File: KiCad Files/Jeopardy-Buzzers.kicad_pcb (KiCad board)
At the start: 2 copper layers, 17 parts, among them U1 CH32V003FxUx, U2 CH340N, U3 NRF24L01_Breakout, U5 AMS1117-3.3, Y1 Crystal_24MHz

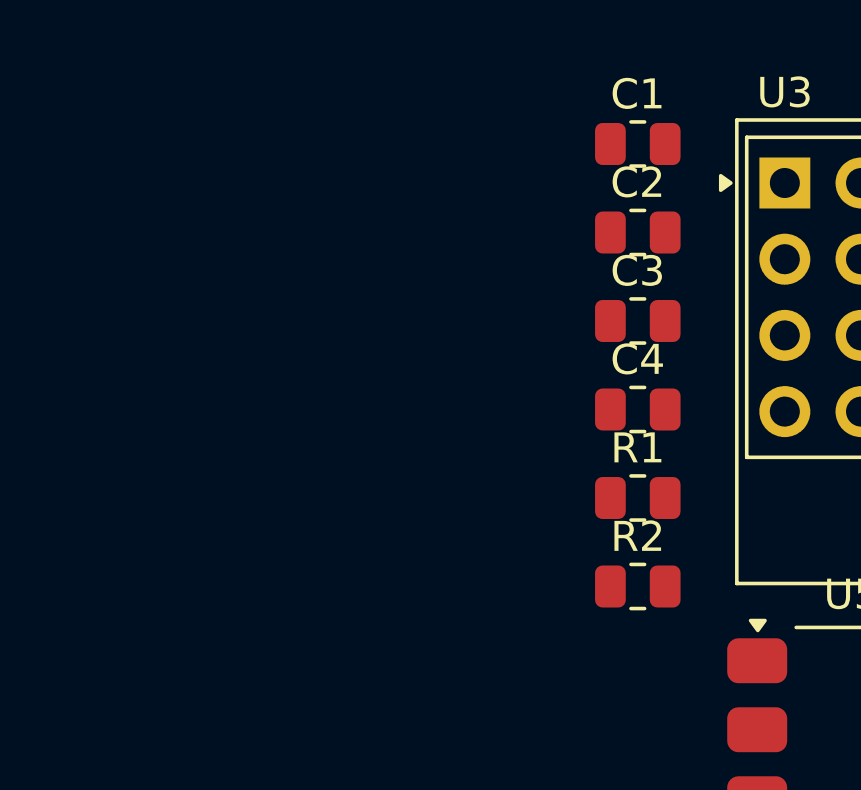
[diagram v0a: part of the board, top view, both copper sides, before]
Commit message: Added step files, and finished usb footprint
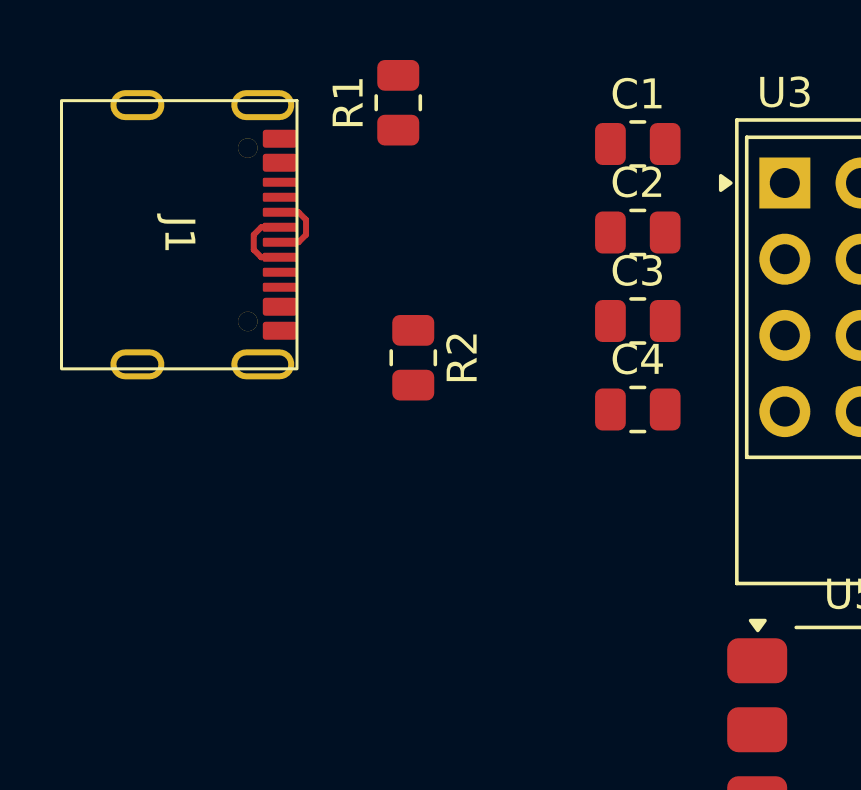
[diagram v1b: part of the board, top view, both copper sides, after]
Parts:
- added J1: USB_C_Receptacle, Library:Usb-C, F.Cu at (22.9, 29.5)
- moved R1 15.4 mm to (26.2, 25.1), turned to 90 degrees
- moved R2 10.7 mm to (26.8, 33.6), turned to -90 degrees
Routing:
- net Net-(D5-K): track 0.00 -> 2.45 mm
- net Net-(D4-K): track 0.00 -> 2.45 mm

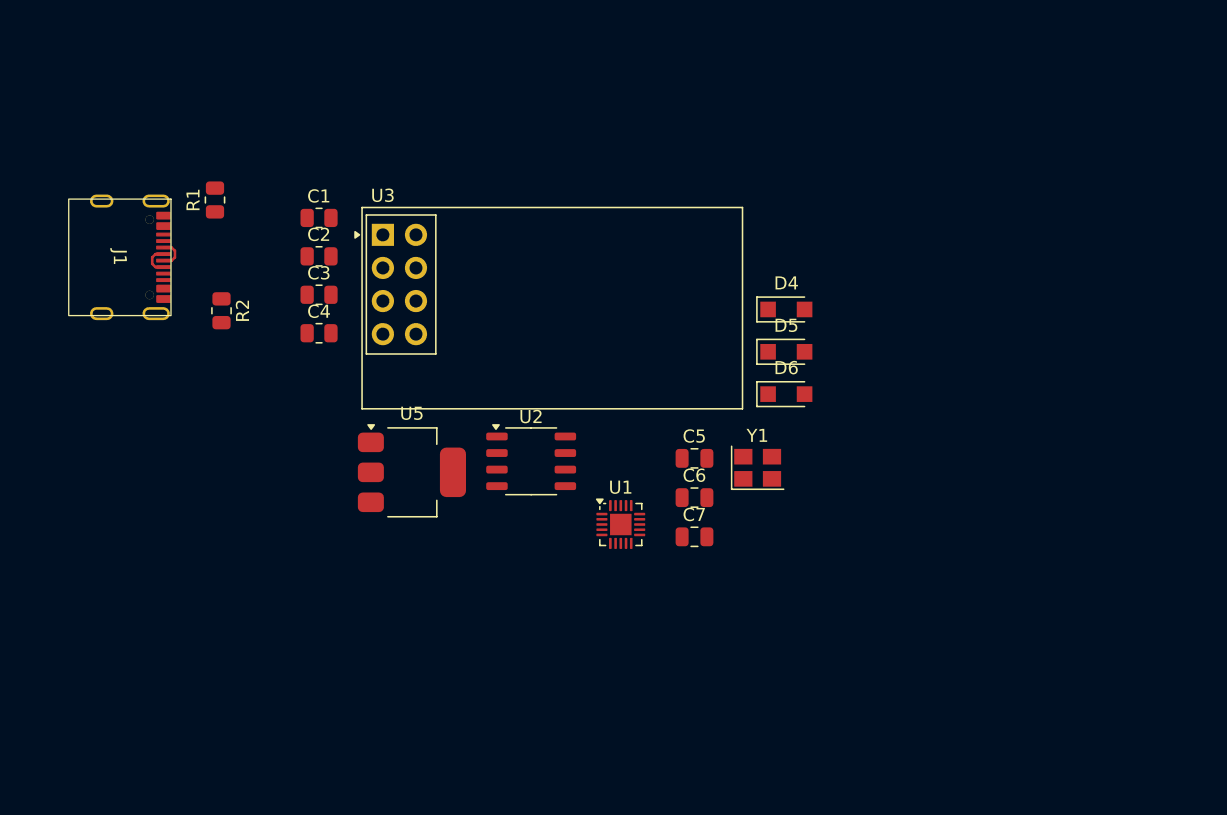
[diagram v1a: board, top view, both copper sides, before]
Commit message: Changed footprints around, also added connectors
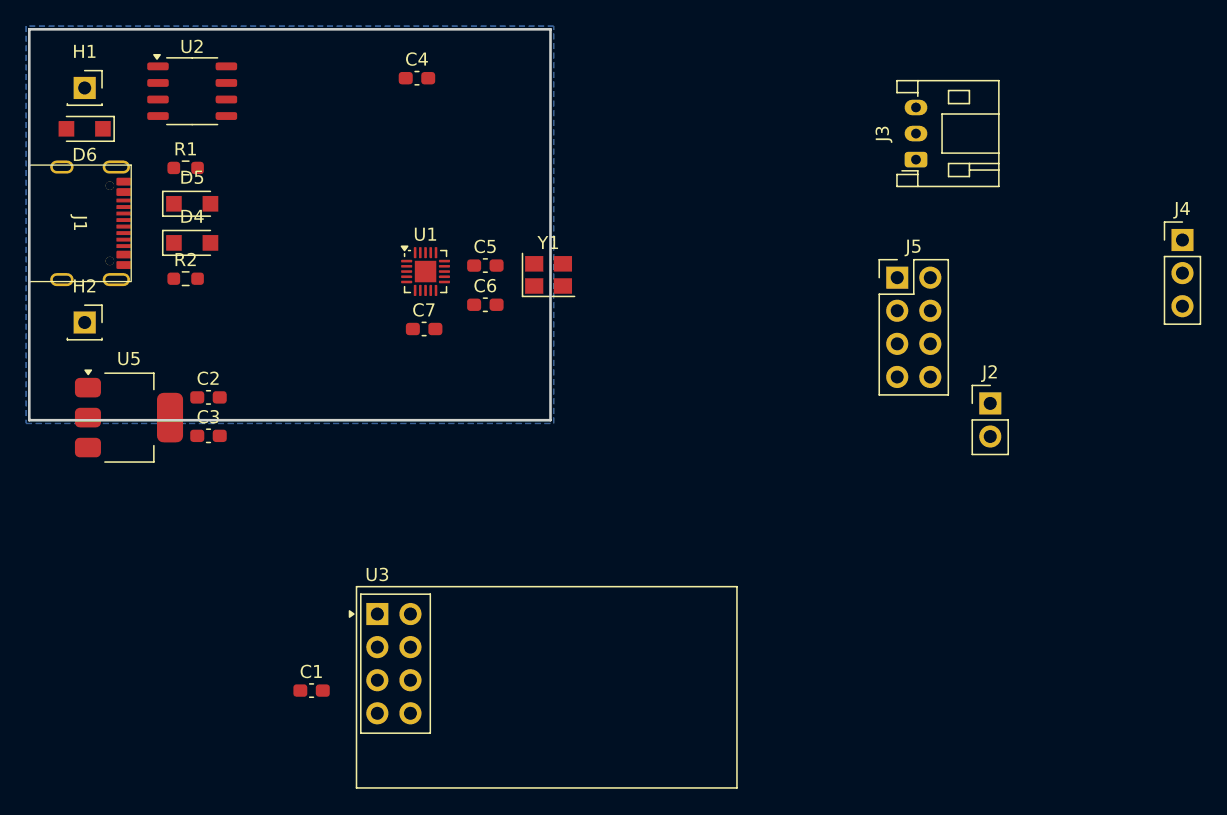
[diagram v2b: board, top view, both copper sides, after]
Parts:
- added H1: MountingHole_Pad, Connector_PinSocket_2.54mm:PinSocket_1x01_P2.54mm_Vertical, F.Cu at (16.2, 16.5)
- added H2: MountingHole_Pad, Connector_PinSocket_2.54mm:PinSocket_1x01_P2.54mm_Vertical, F.Cu at (16.2, 34.5)
- added J2: Conn_01x02_Pin, Connector_PinHeader_2.54mm:PinHeader_1x02_P2.54mm_Vertical, F.Cu at (85.8, 40.7)
- added J3: Conn_01x03_Socket, Connector_JST:JST_PH_S3B-PH-K_1x03_P2.00mm_Horizontal, F.Cu at (80.0, 22.0)
- added J4: Conn_01x03_Socket, Connector_PinHeader_2.54mm:PinHeader_1x03_P2.54mm_Vertical, F.Cu at (100.5, 28.2)
- added J5: Conn_02x04_Odd_Even, Connector_PinHeader_2.54mm:PinHeader_2x04_P2.54mm_Vertical, F.Cu at (78.6, 31.1)
- C1, C2, C3, C4: footprint Resistor_SMD:R_0805_2012Metric -> Capacitor_SMD:C_0603_1608Metric_Pad1.08x0.95mm_HandSolder
- C5, C6, C7: footprint Capacitor_SMD:C_0805_2012Metric -> Capacitor_SMD:C_0603_1608Metric_Pad1.08x0.95mm_HandSolder
- J1: value USB_C_Receptacle -> USB_C_Receptacle_USB2.0_14P
- R1, R2: footprint Resistor_SMD:R_0805_2012Metric -> Resistor_SMD:R_0603_1608Metric_Pad0.98x0.95mm_HandSolder
- moved D6 57.6 mm to (16.2, 19.6), turned to 180 degrees
- moved D5 47.0 mm to (24.5, 25.4)
- moved D4 45.9 mm to (24.5, 28.4)
- moved U2 38.5 mm to (24.5, 16.8)
- moved C1 36.3 mm to (33.7, 62.8)
- moved U3 29.1 mm to (38.7, 56.9)
- moved C7 26.2 mm to (42.3, 35.0)
- moved U1 24.5 mm to (42.4, 30.6)
- moved U5 22.1 mm to (19.6, 41.8)
- moved C5 21.8 mm to (47.0, 30.1)
- moved Y1 21.8 mm to (51.9, 30.9)
- moved C6 21.8 mm to (47.0, 33.1)
- moved C4 21.0 mm to (41.8, 15.8)
- moved C3 13.8 mm to (25.8, 43.2)
- moved C2 13.8 mm to (25.8, 40.2)
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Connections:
- net Net-(D4-K) renamed USB_D+
- net Net-(D5-K) renamed USB_D-
- C7 pad 2: Net-(U1-VDD) -> +5V
- J1 pad A8: unconnected-(J1-SBU1-PadA8) -> (no net)
- J1 pad B8: unconnected-(J1-SBU2-PadB8) -> (no net)
- U1 pad 1: unconnected-(U1-PD7-Pad1) -> WS2812_LED
- U1 pad 10: unconnected-(U1-PC3-Pad10) -> MCU_PC3
- U1 pad 15: unconnected-(U1-PD1-Pad15) -> MCU_SWIO
- U1 pad 16: unconnected-(U1-PD2-Pad16) -> MCU_PD2
- U1 pad 17: unconnected-(U1-PD3-Pad17) -> MCU_PD3
- U1 pad 18: unconnected-(U1-PD4-Pad18) -> MCU_PD4
- U1 pad 5: unconnected-(U1-PD0-Pad5) -> Net-(J2-Pin_2)
- U1 pad 6: Net-(U1-VDD) -> +5V
- U1 pad 8: unconnected-(U1-PC1-Pad8) -> MCU_PC1
- U1 pad 9: unconnected-(U1-PC2-Pad9) -> MCU_PC2
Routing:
- net USB_D-: track 2.45 -> 0.00 mm
- net USB_D+: track 2.45 -> 0.00 mm
- added copper zone on B.Cu, net GND
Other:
- board outline added: 40 x 30 mm

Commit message: moved parts around and started placing planes
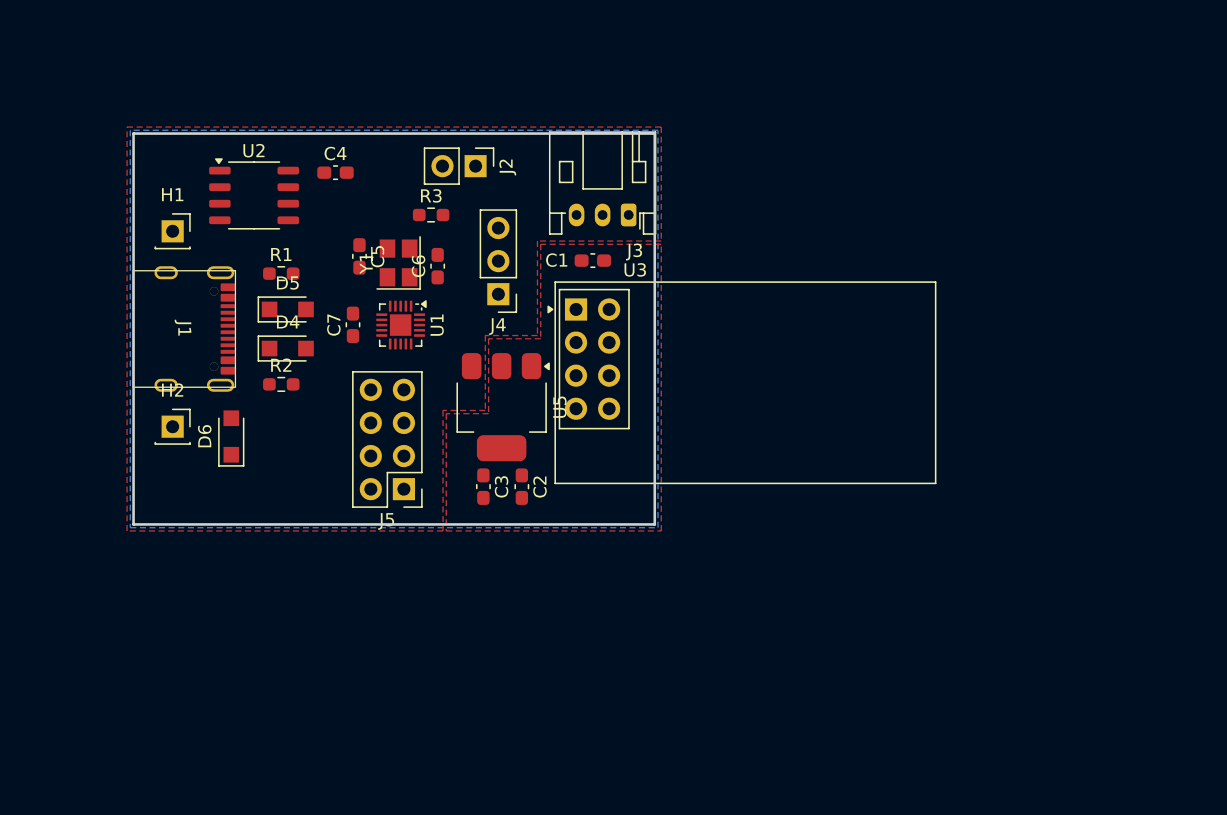
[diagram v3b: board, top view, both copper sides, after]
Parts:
- added R3: 10k, Resistor_SMD:R_0603_1608Metric_Pad0.98x0.95mm_HandSolder, F.Cu at (42.8, 26.2)
- moved J4 52.7 mm to (48.0, 32.3), turned to 180 degrees
- moved J2 43.5 mm to (46.2, 22.5), turned to -90 degrees
- moved J5 41.2 mm to (40.8, 47.3), turned to 180 degrees
- moved C1 39.4 mm to (55.2, 29.8), turned to 180 degrees
- moved U5 28.6 mm to (48.2, 41.0), turned to -90 degrees
- moved U3 27.9 mm to (54.0, 33.5)
- moved D6 26.2 mm to (27.5, 43.2), turned to 90 degrees
- moved C2 25.0 mm to (49.8, 47.1), turned to -90 degrees
- moved J3 22.5 mm to (58.0, 26.2), turned to 180 degrees
- moved C3 21.5 mm to (46.9, 47.1), turned to -90 degrees
- moved H1 12.9 mm to (23.0, 27.5)
- moved Y1 11.5 mm to (40.3, 29.9), turned to 90 degrees
- moved J1 11.4 mm to (27.8, 35.0)
- moved D4 10.9 mm to (31.8, 36.5)
- moved D5 10.9 mm to (31.8, 33.5)
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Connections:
- J5 pad 3: MCU_PC1 -> MCU_PC0
- J5 pad 5: MCU_PC2 -> MCU_PC1
- J5 pad 7: MCU_PC3 -> MCU_PC2
- U1 pad 10: MCU_PC3 -> MCU_SPI_CS
- U1 pad 7: MCU_SPI_CS -> MCU_PC0
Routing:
- added copper zone on F.Cu, net +3V3
- added copper zone on F.Cu, net +5V

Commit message: routed most of the traces, just need to pass ERC/DRC
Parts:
- moved J5 4.30 mm to (41.0, 43.0), turned to -90 degrees
- moved J4 3.72 mm to (49.0, 28.8), turned to 0 degrees
- moved J3 0.56 mm to (57.8, 26.8)
- moved C5 0.55 mm to (37.0, 29.9)
- moved D4 0.51 mm to (32.4, 36.5)
- moved D5 0.51 mm to (32.4, 33.5)
- moved R1 0.51 mm to (31.9, 30.8)
- moved R2 0.51 mm to (31.9, 39.2)
- moved R3 0.51 mm to (42.8, 25.8)
- moved C6 0.45 mm to (43.8, 30.0)
- moved C4 0.25 mm to (35.5, 22.8)
- moved C7 0.23 mm to (36.8, 34.9)
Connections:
- J5 pad 3: MCU_PC0 -> MCU_PC2
- J5 pad 7: MCU_PC2 -> MCU_PC0
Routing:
- net MCU_SPI_CS: track 0.00 -> 31.4 mm
- net MCU_SPI_MOSI: track 0.00 -> 25.2 mm
- net MCU_PD4: track 0.00 -> 25.2 mm, vias 0 -> 1
- net MCU_UART_TX: track 0.00 -> 21.4 mm, vias 0 -> 2
- net NRF24L01_CE: track 0.00 -> 21.2 mm, vias 0 -> 1
- net MCU_PD3: track 0.00 -> 21.1 mm, vias 0 -> 1
- net +5V: track 0.00 -> 19.2 mm
- net MCU_SPI_CLK: track 0.00 -> 18.4 mm, vias 0 -> 1
- net MCU_UART_RX: track 0.00 -> 17.9 mm, vias 0 -> 2
- net WS2812_LED: track 0.00 -> 17.4 mm
- net MCU_PD2: track 0.00 -> 17.1 mm, vias 0 -> 1
- net Net-(J2-Pin_2): track 0.00 -> 16.1 mm, vias 0 -> 2
- net MCU_SPI_MISO: track 0.00 -> 15.6 mm
- net MCU_PC0: track 0.00 -> 13.3 mm
- net MCU_PC1: track 0.00 -> 10.1 mm
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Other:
- board text added: "+5v"
- board text added: "GND"

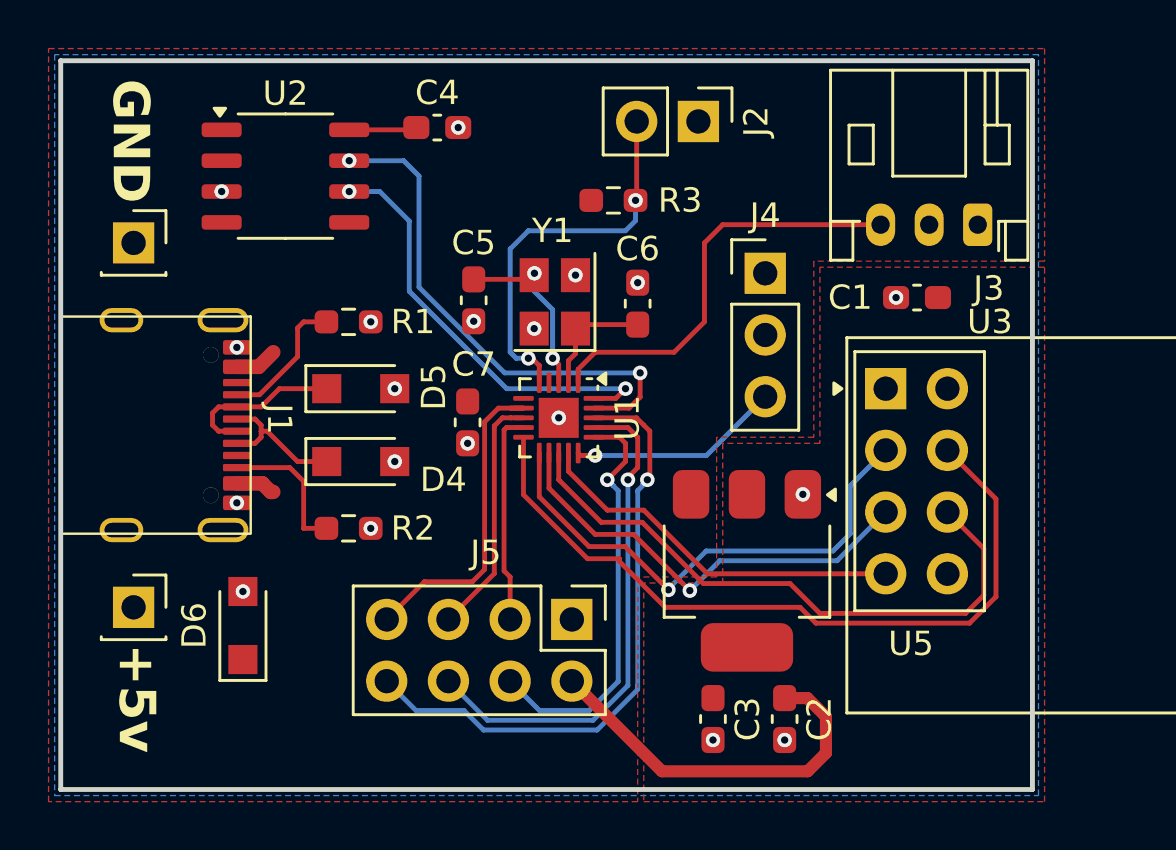
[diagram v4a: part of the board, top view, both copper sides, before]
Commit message: routed the USB and added my logo, text, and version number
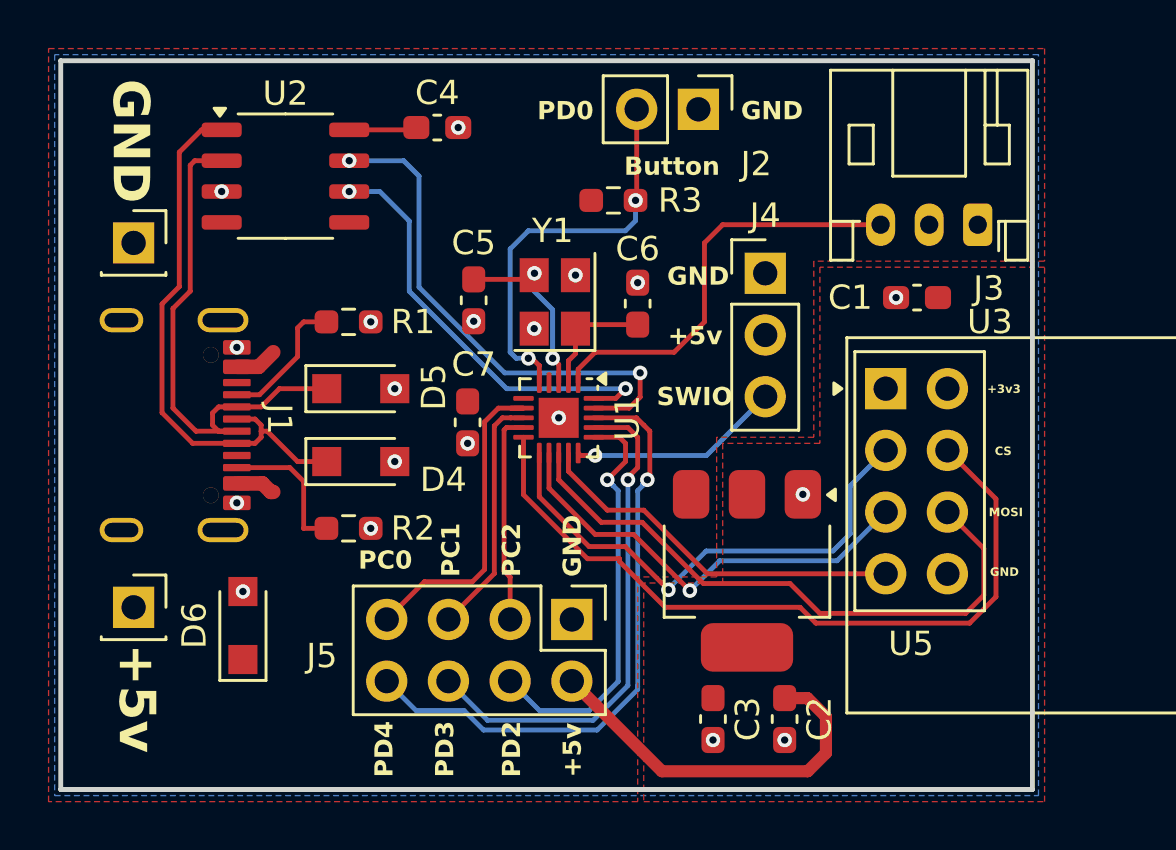
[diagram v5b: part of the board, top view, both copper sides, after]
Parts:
- added G***: LOGO, Library:PCB Logo (12.5x17), B.Cu at (35.5, 29.5)
- moved J2 0.50 mm to (46.2, 22.0)
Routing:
- net USB_D+: track 5.41 -> 22.2 mm
- net USB_D-: track 6.21 -> 20.9 mm
- net Net-(J2-Pin_2): track 16.1 -> 16.6 mm
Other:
- board text added: "+3v3"
- board text added: "Button"
- board text added: "CS"
- board text added: "Devin Marx"
- board text added: "Jeopardy Buzzer Control Board"
- board text added: "MOSI"
- board text added: "PC0"
- board text added: "PC1"
- board text added: "PC2"
- board text added: "PD0"
- board text added: "PD2"
- board text added: "PD3"
- board text added: "PD4"
- board text added: "SWIO"
- board text added: "V0.1"
